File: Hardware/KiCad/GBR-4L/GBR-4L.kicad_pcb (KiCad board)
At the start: 4 copper layers, 160 x 100 mm, 188 parts, among them J1 USB4105-GF-A, J101 EM7565 M.2 Key B socket, J102 MODEM_CONTROL, J201 EM7565 M.2 Key B socket, J202 MODEM_CONTROL, J301 EM7565 M.2 Key B socket, J302 MODEM_CONTROL, J401 EM7565 M.2 Key B socket, J402 MODEM_CONTROL, J511 2452808-1 nano-SIM, J521 2452808-1 nano-SIM, J531 2452808-1 nano-SIM, J541 2452808-1 nano-SIM, J701 12V INPUT 5A, Q701 30V P-MOSFET low-RDS(on), Q911 MMBT3906, Q921 MMBT3906, Q931 MMBT3906, Q941 MMBT3906, SW911 MODEM 1 RESET, SW912 MODEM 1 RF DISABLE, SW921 MODEM 2 RESET, SW922 MODEM 2 RF DISABLE, SW931 MODEM 3 RESET, SW932 MODEM 3 RF DISABLE, SW941 MODEM 4 RESET, SW942 MODEM 4 RF DISABLE, U1 USBLC6-2SC6, U11 LOW-CAP SIM ESD ARRAY, U12 LOW-CAP SIM ESD ARRAY, U13 LOW-CAP SIM ESD ARRAY, U14 LOW-CAP SIM ESD ARRAY, U2 USB2514Bi-I/M2, U21 TPS56339DDCR, U22 TPS56339DDCR, U23 TPS56339DDCR, U24 TPS56339DDCR, U25 TPS56339DDCR, Y1 24MHz

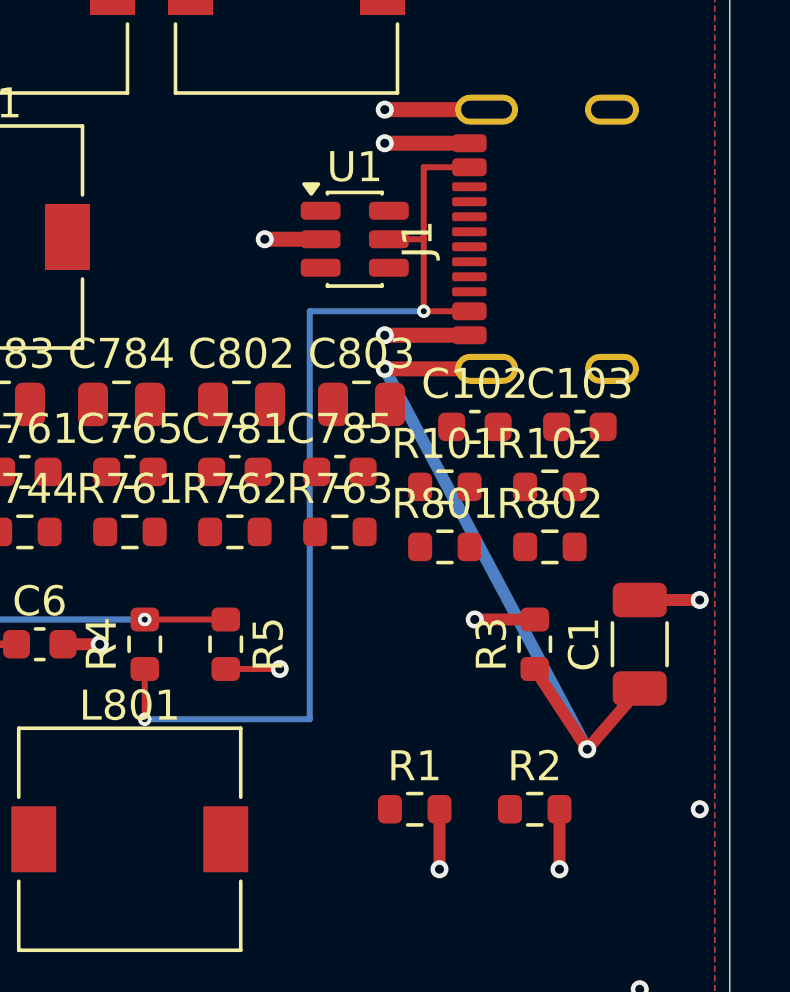
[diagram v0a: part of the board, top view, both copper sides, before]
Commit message: Route USB Type-C CC pull-downs
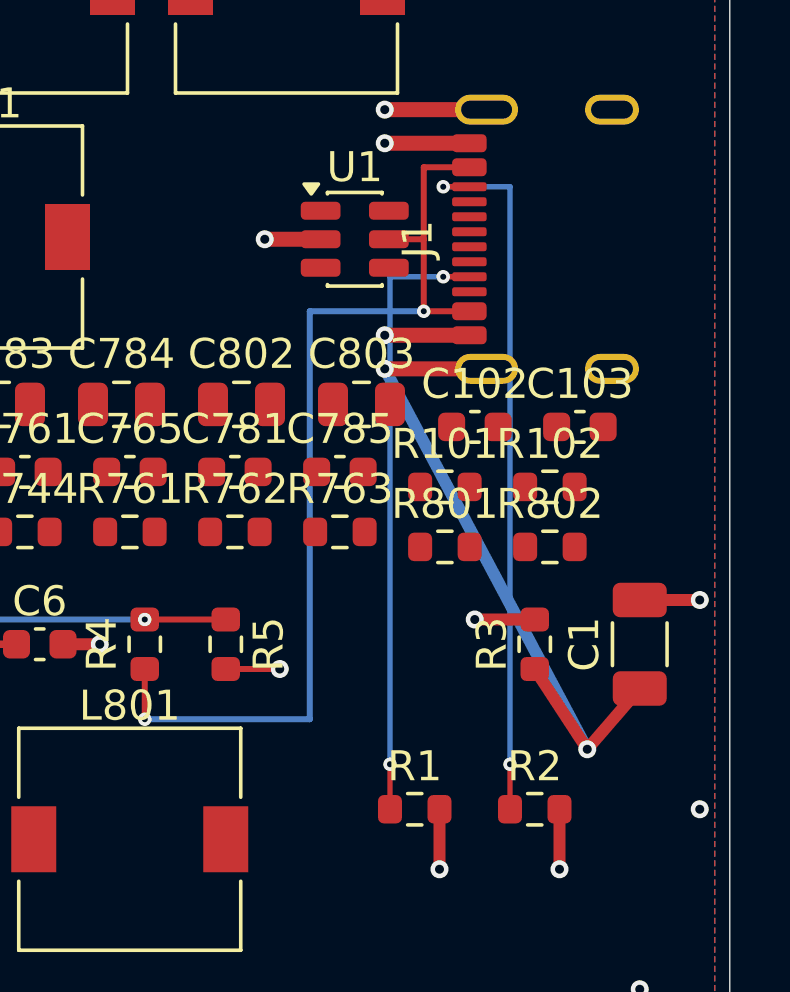
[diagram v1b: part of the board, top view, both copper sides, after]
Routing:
- net USB_CC2: track 0.00 -> 23.8 mm, vias 0 -> 2
- net USB_CC1: track 0.00 -> 20.4 mm, vias 0 -> 2
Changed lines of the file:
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@@
+	)
+	(segment
+		(start 168.675 52.5)
+		(end 168.675 54)
+		(width 0.18)
+		(layer "F.Cu")
+		(net "USB_CC1")
+	)
+	(segment
+		(start 171.32 36.25)
+		(end 170.45 36.25)
+		(width 0.18)
+		(layer "F.Cu")
+		(net "USB_CC1")
+	)
+	(via
+		(at 170.45 36.25)
+		(size 0.45)
+		(drill 0.2)
+		(layers "F.Cu" "B.Cu")
+		(net "USB_CC1")
+	)
+	(via
+		(at 168.675 52.5)
+		(size 0.45)
+		(drill 0.2)
+		(layers "F.Cu" "B.Cu")
+		(net "USB_CC1")
+	)
+	(segment
+		(start 168.675 36.25)
+		(end 168.675 52.5)
+		(width 0.18)
+		(layer "B.Cu")
+		(net "USB_CC1")
+	)
+	(segment
+		(start 170.45 36.25)
+		(end 168.675 36.25)
+		(width 0.18)
+		(layer "B.Cu")
+		(net "USB_CC1")
+	)
+	(segment
+		(start 171.32 33.25)
+		(end 170.45 33.25)
+		(width 0.18)
+		(layer "F.Cu")
+		(net "USB_CC2")
+	)
+	(segment
+		(start 172.675 52.5)
+		(end 172.675 54)
+		(width 0.18)
+		(layer "F.Cu")
+		(net "USB_CC2")
+	)
+	(via
+		(at 170.45 33.25)
+		(size 0.45)
+		(drill 0.2)
+		(layers "F.Cu" "B.Cu")
+		(net "USB_CC2")
+	)
+	(via
+		(at 172.675 52.5)
+		(size 0.45)
+		(drill 0.2)
+		(layers "F.Cu" "B.Cu")
+		(net "USB_CC2")
+	)
+	(segment
+		(start 172.675 33.25)
+		(end 172.675 52.5)
+		(width 0.18)
+		(layer "B.Cu")
+		(net "USB_CC2")
+	)
+	(segment
+		(start 170.45 33.25)
+		(end 172.675 33.25)
+		(width 0.18)
+		(layer "B.Cu")
+		(net "USB_CC2")
 	)
 	(segment

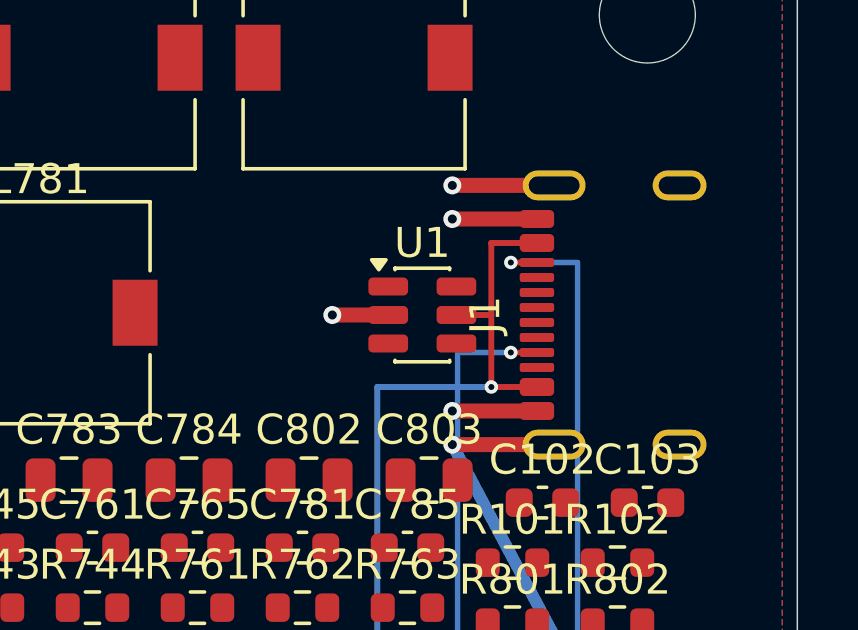
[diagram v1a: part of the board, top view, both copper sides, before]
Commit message: Route USB connector pair to ESD clamp
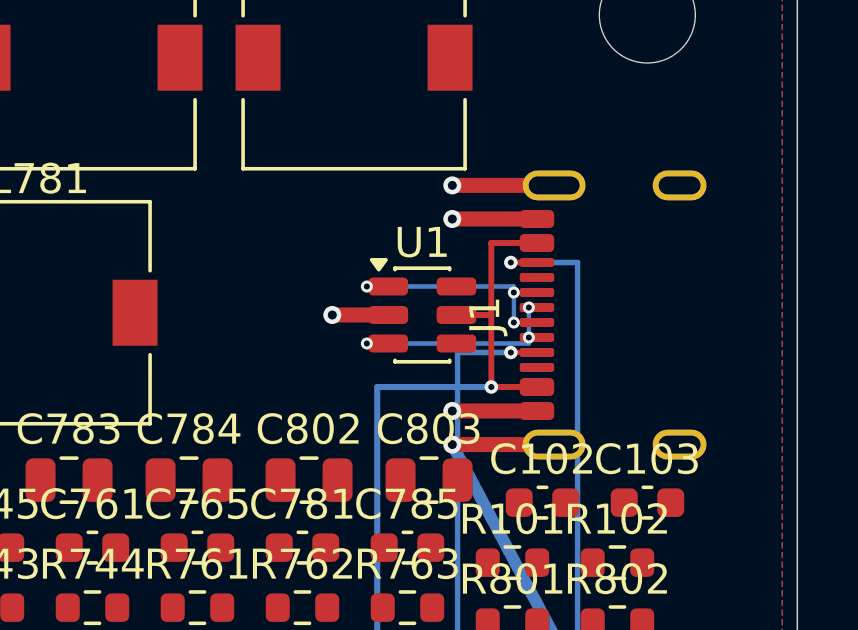
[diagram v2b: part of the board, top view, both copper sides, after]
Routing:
- net USB_UP_DP_CONN: track 0.00 -> 8.35 mm, vias 0 -> 3
- net USB_UP_DM_CONN: track 0.00 -> 7.85 mm, vias 0 -> 3
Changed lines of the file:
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@@
+	)
+	(segment
+		(start 171.32 35.25)
+		(end 170.55 35.25)
+		(width 0.15)
+		(layer "F.Cu")
+		(net "USB_UP_DP_CONN")
+	)
+	(segment
+		(start 166.363 34.05)
+		(end 165.65 34.05)
+		(width 0.15)
+		(layer "F.Cu")
+		(net "USB_UP_DP_CONN")
+	)
+	(segment
+		(start 171.32 34.25)
+		(end 170.55 34.25)
+		(width 0.15)
+		(layer "F.Cu")
+		(net "USB_UP_DP_CONN")
+	)
+	(via
+		(at 170.55 34.25)
+		(size 0.4)
+		(drill 0.2)
+		(layers "F.Cu" "B.Cu")
+		(net "USB_UP_DP_CONN")
+	)
+	(via
+		(at 165.65 34.05)
+		(size 0.4)
+		(drill 0.2)
+		(layers "F.Cu" "B.Cu")
+		(net "USB_UP_DP_CONN")
+	)
+	(via
+		(at 170.55 35.25)
+		(size 0.4)
+		(drill 0.2)
+		(layers "F.Cu" "B.Cu")
+		(net "USB_UP_DP_CONN")
+	)
+	(segment
+		(start 170.55 34.25)
+		(end 170.55 35.25)
+		(width 0.15)
+		(layer "B.Cu")
+		(net "USB_UP_DP_CONN")
+	)
+	(segment
+		(start 165.65 34.05)
+		(end 170.55 34.05)
+		(width 0.15)
+		(layer "B.Cu")
+		(net "USB_UP_DP_CONN")
+	)
+	(segment
+		(start 170.55 34.05)
+		(end 170.55 34.25)
+		(width 0.15)
+		(layer "B.Cu")
+		(net "USB_UP_DP_CONN")
+	)
+	(segment
+		(start 171.32 35.75)
+		(end 171.05 35.75)
+		(width 0.15)
+		(layer "F.Cu")
+		(net "USB_UP_DM_CONN")
+	)
+	(segment
+		(start 171.32 34.75)
+		(end 171.05 34.75)
+		(width 0.15)
+		(layer "F.Cu")
+		(net "USB_UP_DM_CONN")
+	)
+	(segment
+		(start 166.363 35.95)
+		(end 165.65 35.95)
+		(width 0.15)
+		(layer "F.Cu")
+		(net "USB_UP_DM_CONN")
+	)
+	(via
+		(at 171.05 35.75)
+		(size 0.4)
+		(drill 0.2)
+		(layers "F.Cu" "B.Cu")
+		(net "USB_UP_DM_CONN")
+	)
+	(via
+		(at 171.05 34.75)
+		(size 0.4)
+		(drill 0.2)
+		(layers "F.Cu" "B.Cu")
+		(net "USB_UP_DM_CONN")
+	)
+	(via
+		(at 165.65 35.95)
+		(size 0.4)
+		(drill 0.2)
+		(layers "F.Cu" "B.Cu")
+		(net "USB_UP_DM_CONN")
+	)
+	(segment
+		(start 171.05 35.95)
+		(end 171.05 35.75)
+		(width 0.15)
+		(layer "B.Cu")
+		(net "USB_UP_DM_CONN")
+	)
+	(segment
+		(start 165.65 35.95)
+		(end 171.05 35.95)
+		(width 0.15)
+		(layer "B.Cu")
+		(net "USB_UP_DM_CONN")
+	)
+	(segment
+		(start 171.05 35.75)
+		(end 171.05 34.75)
+		(width 0.15)
+		(layer "B.Cu")
+		(net "USB_UP_DM_CONN")
 	)
 	(segment

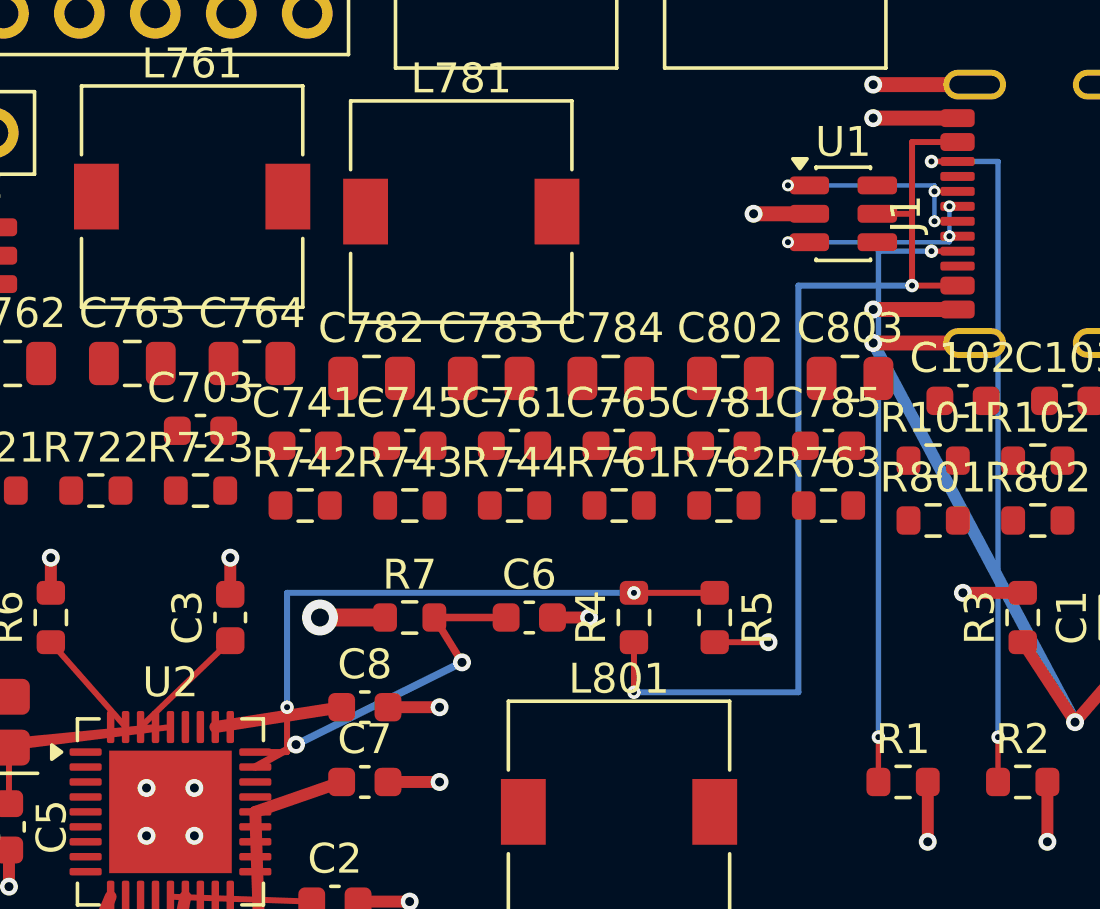
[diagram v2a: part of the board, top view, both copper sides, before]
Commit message: Route upstream USB pair to hub
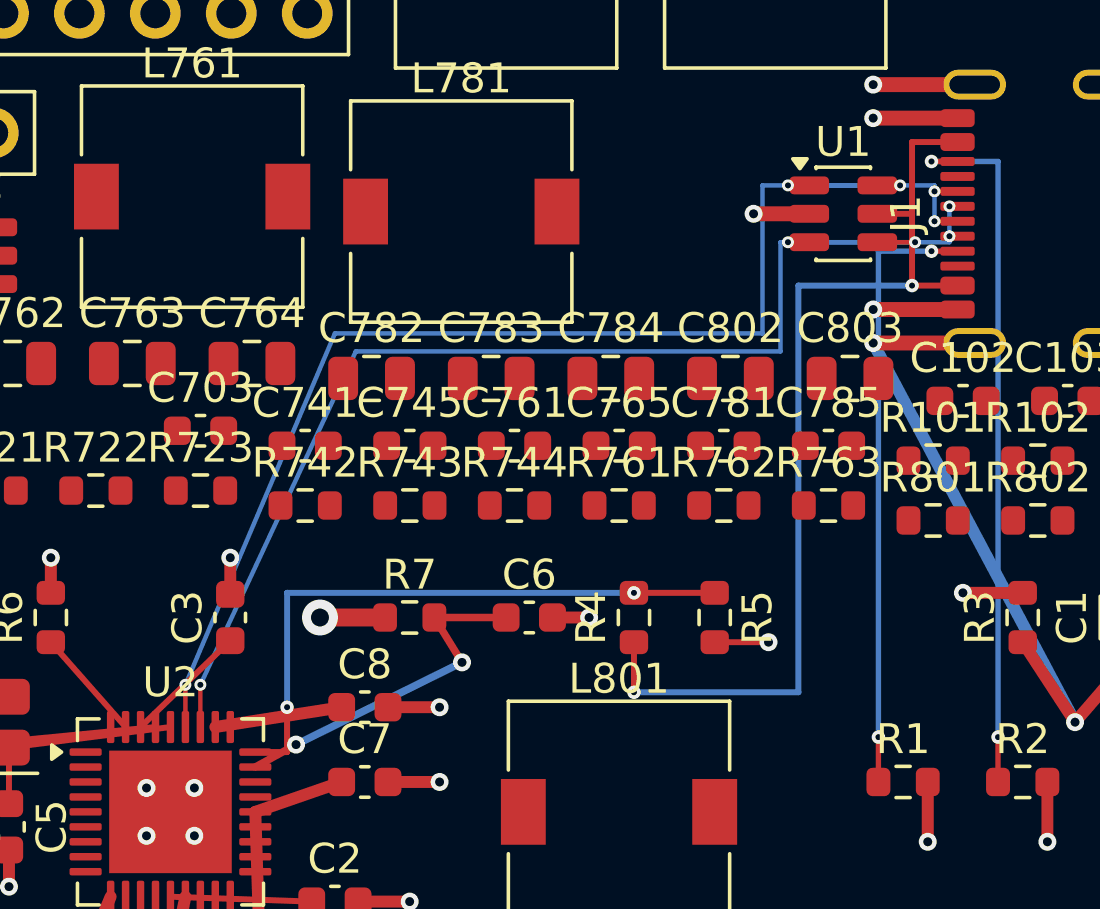
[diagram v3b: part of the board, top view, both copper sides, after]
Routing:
- net USB_UP_DP: track 0.00 -> 38.8 mm, vias 0 -> 2
- net USB_UP_DM: track 0.00 -> 37.3 mm, vias 0 -> 2
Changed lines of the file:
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@@
+	)
+	(segment
+		(start 168.637 35.95)
+		(end 169.9 35.95)
+		(width 0.15)
+		(layer "F.Cu")
+		(net "USB_UP_DM")
+	)
+	(segment
+		(start 146 50.75)
+		(end 146 52.163)
+		(width 0.15)
+		(layer "F.Cu")
+		(net "USB_UP_DM")
+	)
+	(via
+		(at 169.9 35.95)
+		(size 0.4)
+		(drill 0.2)
+		(layers "F.Cu" "B.Cu")
+		(net "USB_UP_DM")
+	)
+	(via
+		(at 146 50.75)
+		(size 0.4)
+		(drill 0.2)
+		(layers "F.Cu" "B.Cu")
+		(net "USB_UP_DM")
+	)
+	(segment
+		(start 165.4 39.6)
+		(end 151.2 39.6)
+		(width 0.15)
+		(layer "B.Cu")
+		(net "USB_UP_DM")
+	)
+	(segment
+		(start 165.4 35.95)
+		(end 165.4 39.6)
+		(width 0.15)
+		(layer "B.Cu")
+		(net "USB_UP_DM")
+	)
+	(segment
+		(start 151.2 39.6)
+		(end 146 50.75)
+		(width 0.15)
+		(layer "B.Cu")
+		(net "USB_UP_DM")
+	)
+	(segment
+		(start 169.9 35.95)
+		(end 165.4 35.95)
+		(width 0.15)
+		(layer "B.Cu")
+		(net "USB_UP_DM")
 	)
 	(segment
@@
 	)
 	(segment
+		(start 145.5 50.75)
+		(end 145.5 52.163)
+		(width 0.15)
+		(layer "F.Cu")
+		(net "USB_UP_DP")
+	)
+	(segment
+		(start 168.637 34.05)
+		(end 169.4 34.05)
+		(width 0.15)
+		(layer "F.Cu")
+		(net "USB_UP_DP")
+	)
+	(via
+		(at 145.5 50.75)
+		(size 0.4)
+		(drill 0.2)
+		(layers "F.Cu" "B.Cu")
+		(net "USB_UP_DP")
+	)
+	(via
+		(at 169.4 34.05)
+		(size 0.4)
+		(drill 0.2)
+		(layers "F.Cu" "B.Cu")
+		(net "USB_UP_DP")
+	)
+	(segment
+		(start 164.8 39)
+		(end 150.5 39)
+		(width 0.15)
+		(layer "B.Cu")
+		(net "USB_UP_DP")
+	)
+	(segment
+		(start 164.8 34.05)
+		(end 164.8 39)
+		(width 0.15)
+		(layer "B.Cu")
+		(net "USB_UP_DP")
+	)
+	(segment
+		(start 150.5 39)
+		(end 145.5 50.75)
+		(width 0.15)
+		(layer "B.Cu")
+		(net "USB_UP_DP")
+	)
+	(segment
+		(start 169.4 34.05)
+		(end 164.8 34.05)
+		(width 0.15)
+		(layer "B.Cu")
+		(net "USB_UP_DP")
+	)
+	(segment

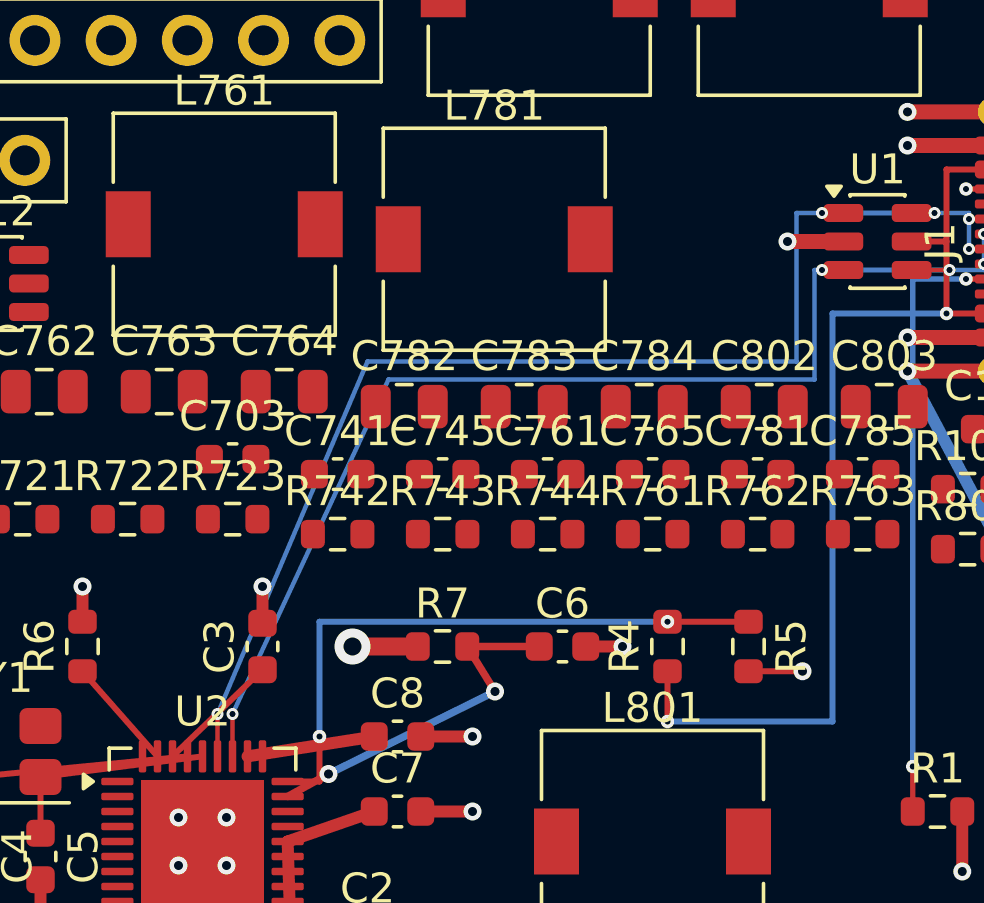
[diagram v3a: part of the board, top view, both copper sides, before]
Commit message: Add USB upstream return vias
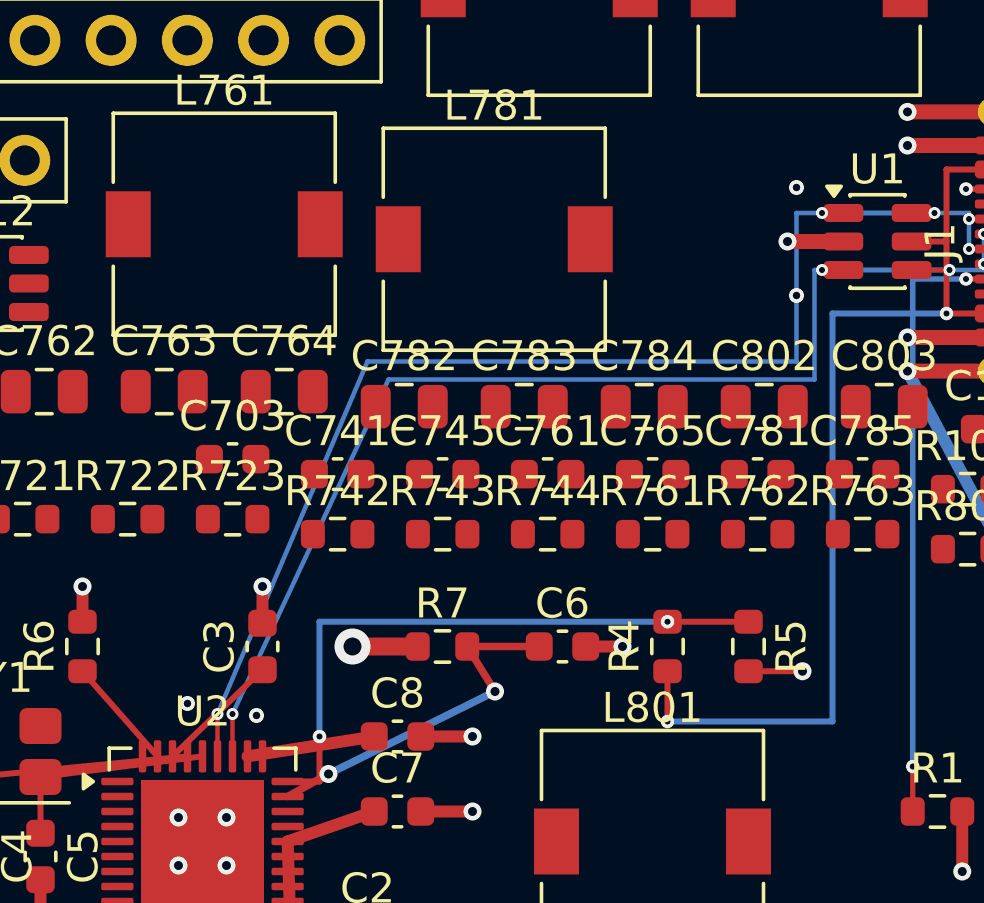
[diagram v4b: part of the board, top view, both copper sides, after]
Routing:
- net GND: vias 67 -> 71
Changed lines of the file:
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@@
+	)
+	(via
+		(at 164.8 36.8)
+		(size 0.5)
+		(drill 0.25)
+		(layers "F.Cu" "B.Cu")
+		(net "GND")
 	)
 	(via
@@
 	)
 	(via
+		(at 144.5 50.4)
+		(size 0.5)
+		(drill 0.25)
+		(layers "F.Cu" "B.Cu")
+		(net "GND")
+	)
+	(via
 		(at 145.8 55.8)
 		(size 0.6)
@@
 		(layers "F.Cu" "B.Cu")
 		(net "GND")
+	)
+	(via
+		(at 146.8 50.8)
+		(size 0.5)
+		(drill 0.25)
+		(layers "F.Cu" "B.Cu")
+		(net "GND")
+	)
+	(via
+		(at 164.8 33.2)
+		(size 0.5)
+		(drill 0.25)
+		(layers "F.Cu" "B.Cu")
+		(net "GND")
